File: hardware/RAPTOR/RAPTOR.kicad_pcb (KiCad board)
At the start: 2 copper layers, 101.6 x 53.3 mm, 13 parts, among them P1 Digital, P10 CONN_01X01, P11 CONN_01X01, P12 CONN_01X01, P13 CONN_01X01, P2 Power, P3 Analog, P4 Analog, P5 PWM, P6 PWM, P7 Communication, P8 CONN_01X01, P9 CONN_01X01

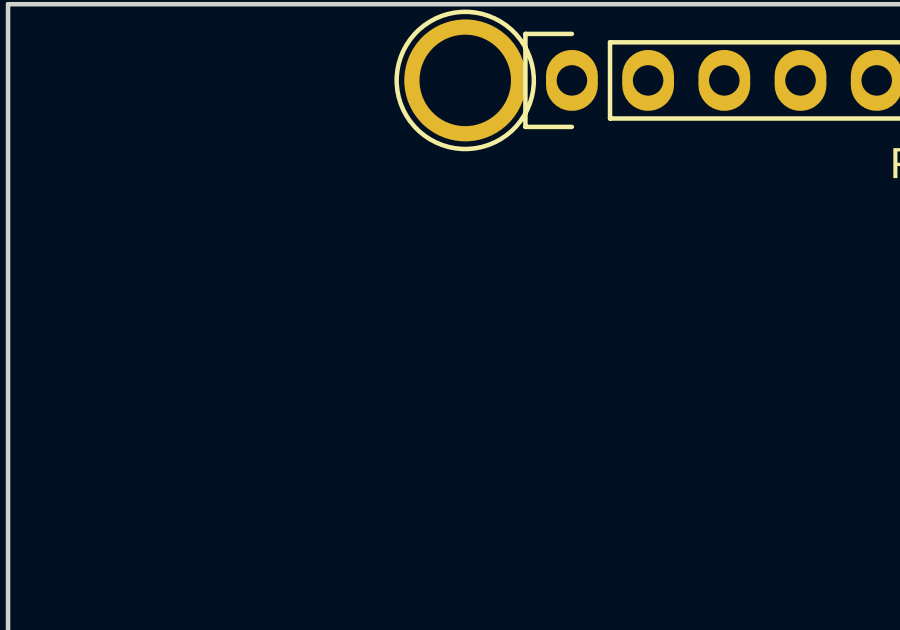
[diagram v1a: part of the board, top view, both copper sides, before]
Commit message: add bmp footprint to pcb
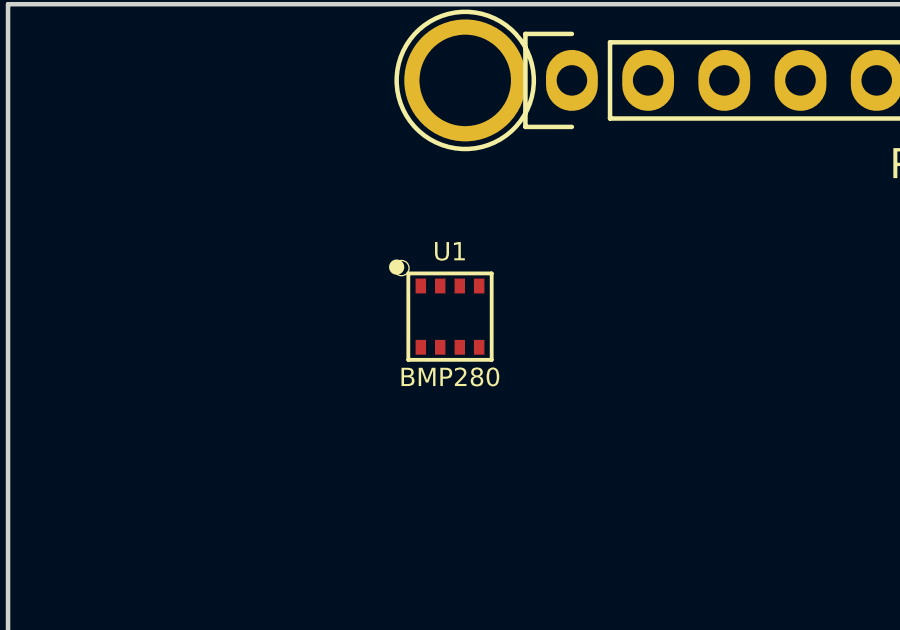
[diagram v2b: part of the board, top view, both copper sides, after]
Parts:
- added U1: BMP280, Silicon-Standard:LGA-8-2.5X2.5, F.Cu at (118.1, 78.7)
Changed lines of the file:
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@@
     (tracks 0)
     (zones 0)
-    (modules 13)
-    (nets 87)
+    (modules 14)
+    (nets 89)
   )
   (page A4)
@@
   (net 85 "/18(Tx1)")
   (net 86 "/19(Rx1)")
+  (net 87 "Net-(U1-Pad2)")
+  (net 88 "Net-(U1-Pad5)")
   (net_class Default "This is the default net class."
     (clearance 0.2)
@@
     (add_net "Net-(P8-Pad1)")
     (add_net "Net-(P9-Pad1)")
+    (add_net "Net-(U1-Pad2)")
+    (add_net "Net-(U1-Pad5)")
   )
   (module Socket_Arduino_Mega:Socket_Strip_Arduino_2x18 locked (layer F.Cu)
@@
       (net 76 "Net-(P13-Pad1)"))
   )
+  (module Silicon-Standard:LGA-8-2.5X2.5 (layer F.Cu)
+    (at 118.11 78.74)
+    (descr "LGA 8-PIN &NDASH;  2.5MM X 2.5MM, 0.65MM PITCH")
+    (tags "LGA 8-PIN &NDASH;  2.5MM X 2.5MM, 0.65MM PITCH")
+    (attr smd)
+    (fp_text reference U1 (at 0 -2.159) (layer F.SilkS)
+      (effects (font (size 0.6096 0.6096) (thickness 0.127)))
+    )
+    (fp_text value BMP280 (at 0 2.032) (layer F.SilkS)
+      (effects (font (size 0.6096 0.6096) (thickness 0.127)))
+    )
+    (fp_circle (center -1.778 -1.651) (end -1.651 -1.651) (layer F.SilkS) (width 0.254))
+    (fp_line (start -1.14808 -0.79756) (end -0.79756 -0.79756) (layer Dwgs.User) (width 0.06604))
+    (fp_line (start -0.79756 -0.79756) (end -0.79756 -1.14808) (layer Dwgs.User) (width 0.06604))
+    (fp_line (start -1.14808 -1.14808) (end -0.79756 -1.14808) (layer Dwgs.User) (width 0.06604))
+    (fp_line (start -1.14808 -0.79756) (end -1.14808 -1.14808) (layer Dwgs.User) (width 0.06604))
+    (fp_line (start -0.49784 -0.79756) (end -0.14986 -0.79756) (layer Dwgs.User) (width 0.06604))
+    (fp_line (start -0.14986 -0.79756) (end -0.14986 -1.14808) (layer Dwgs.User) (width 0.06604))
+    (fp_line (start -0.49784 -1.14808) (end -0.14986 -1.14808) (layer Dwgs.User) (width 0.06604))
+    (fp_line (start -0.49784 -0.79756) (end -0.49784 -1.14808) (layer Dwgs.User) (width 0.06604))
+    (fp_line (start 0.14986 -0.79756) (end 0.49784 -0.79756) (layer Dwgs.User) (width 0.06604))
+    (fp_line (start 0.49784 -0.79756) (end 0.49784 -1.14808) (layer Dwgs.User) (width 0.06604))
+    (fp_line (start 0.14986 -1.14808) (end 0.49784 -1.14808) (layer Dwgs.User) (width 0.06604))
+    (fp_line (start 0.14986 -0.79756) (end 0.14986 -1.14808) (layer Dwgs.User) (width 0.06604))
+    (fp_line (start 0.79756 -0.79756) (end 1.14808 -0.79756) (layer Dwgs.User) (width 0.06604))
+    (fp_line (start 1.14808 -0.79756) (end 1.14808 -1.14808) (layer Dwgs.User) (width 0.06604))
+    (fp_line (start 0.79756 -1.14808) (end 1.14808 -1.14808) (layer Dwgs.User) (width 0.06604))
+    (fp_line (start 0.79756 -0.79756) (end 0.79756 -1.14808) (layer Dwgs.User) (width 0.06604))
+    (fp_line (start -1.14808 1.14808) (end -0.79756 1.14808) (layer Dwgs.User) (width 0.06604))
+    (fp_line (start -0.79756 1.14808) (end -0.79756 0.79756) (layer Dwgs.User) (width 0.06604))
+    (fp_line (start -1.14808 0.79756) (end -0.79756 0.79756) (layer Dwgs.User) (width 0.06604))
+    (fp_line (start -1.14808 1.14808) (end -1.14808 0.79756) (layer Dwgs.User) (width 0.06604))
+    (fp_line (start -0.49784 1.14808) (end -0.14986 1.14808) (layer Dwgs.User) (width 0.06604))
+    (fp_line (start -0.14986 1.14808) (end -0.14986 0.79756) (layer Dwgs.User) (width 0.06604))
+    (fp_line (start -0.49784 0.79756) (end -0.14986 0.79756) (layer Dwgs.User) (width 0.06604))
+    (fp_line (start -0.49784 1.14808) (end -0.49784 0.79756) (layer Dwgs.User) (width 0.06604))
+    (fp_line (start 0.14986 1.14808) (end 0.49784 1.14808) (layer Dwgs.User) (width 0.06604))
+    (fp_line (start 0.49784 1.14808) (end 0.49784 0.79756) (layer Dwgs.User) (width 0.06604))
+    (fp_line (start 0.14986 0.79756) (end 0.49784 0.79756) (layer Dwgs.User) (width 0.06604))
+    (fp_line (start 0.14986 1.14808) (end 0.14986 0.79756) (layer Dwgs.User) (width 0.06604))
+    (fp_line (start 0.79756 1.14808) (end 1.14808 1.14808) (layer Dwgs.User) (width 0.06604))
+    (fp_line (start 1.14808 1.14808) (end 1.14808 0.79756) (layer Dwgs.User) (width 0.06604))
+    (fp_line (start 0.79756 0.79756) (end 1.14808 0.79756) (layer Dwgs.User) (width 0.06604))
+    (fp_line (start 0.79756 1.14808) (end 0.79756 0.79756) (layer Dwgs.User) (width 0.06604))
+    (fp_line (start -1.38938 1.44018) (end -1.38938 -1.44018) (layer F.SilkS) (width 0.127))
+    (fp_line (start -1.38938 -1.44018) (end 1.38938 -1.44018) (layer F.SilkS) (width 0.127))
+    (fp_line (start 1.38938 -1.44018) (end 1.38938 1.44018) (layer F.SilkS) (width 0.127))
+    (fp_line (start 1.38938 1.44018) (end -1.38938 1.44018) (layer F.SilkS) (width 0.127))
+    (fp_line (start 1.24968 1.24968) (end 1.24968 -1.24968) (layer Dwgs.User) (width 0))
+    (fp_line (start 1.24968 -1.24968) (end -1.24968 -1.24968) (layer Dwgs.User) (width 0))
+    (fp_line (start -1.24968 -1.24968) (end -1.24968 1.24968) (layer Dwgs.User) (width 0))
+    (fp_line (start -1.24968 1.24968) (end 1.24968 1.24968) (layer Dwgs.User) (width 0))
+    (fp_circle (center -1.61798 -1.61798) (end -1.61798 -1.87198) (layer F.SilkS) (width 0))
+    (pad 1 smd rect (at -0.97282 -1.02362 90) (size 0.49784 0.34798) (layers F.Cu F.Paste F.Mask)
+      (net 1 GND) (solder_mask_margin 0.1016))
+    (pad 2 smd rect (at -0.32258 -1.02362 90) (size 0.49784 0.34798) (layers F.Cu F.Paste F.Mask)
+      (net 87 "Net-(U1-Pad2)") (solder_mask_margin 0.1016))
+    (pad 3 smd rect (at 0.32258 -1.02362 90) (size 0.49784 0.34798) (layers F.Cu F.Paste F.Mask)
+      (net 69 "/20(SDA)") (solder_mask_margin 0.1016))
+    (pad 4 smd rect (at 0.97282 -1.02362 90) (size 0.49784 0.34798) (layers F.Cu F.Paste F.Mask)
+      (net 70 "/21(SCL)") (solder_mask_margin 0.1016))
+    (pad 5 smd rect (at 0.97282 1.02362 90) (size 0.49784 0.34798) (layers F.Cu F.Paste F.Mask)
+      (net 88 "Net-(U1-Pad5)") (solder_mask_margin 0.1016))
+    (pad 6 smd rect (at 0.32258 1.02362 90) (size 0.49784 0.34798) (layers F.Cu F.Paste F.Mask)
+      (net 34 +5V) (solder_mask_margin 0.1016))
+    (pad 7 smd rect (at -0.32258 1.02362 90) (size 0.49784 0.34798) (layers F.Cu F.Paste F.Mask)
+      (net 1 GND) (solder_mask_margin 0.1016))
+    (pad 8 smd rect (at -0.97282 1.02362 90) (size 0.49784 0.34798) (layers F.Cu F.Paste F.Mask)
+      (net 34 +5V) (solder_mask_margin 0.1016))
+  )
   (gr_text 1 (at 131.318 116.586 90) (layer F.SilkS)

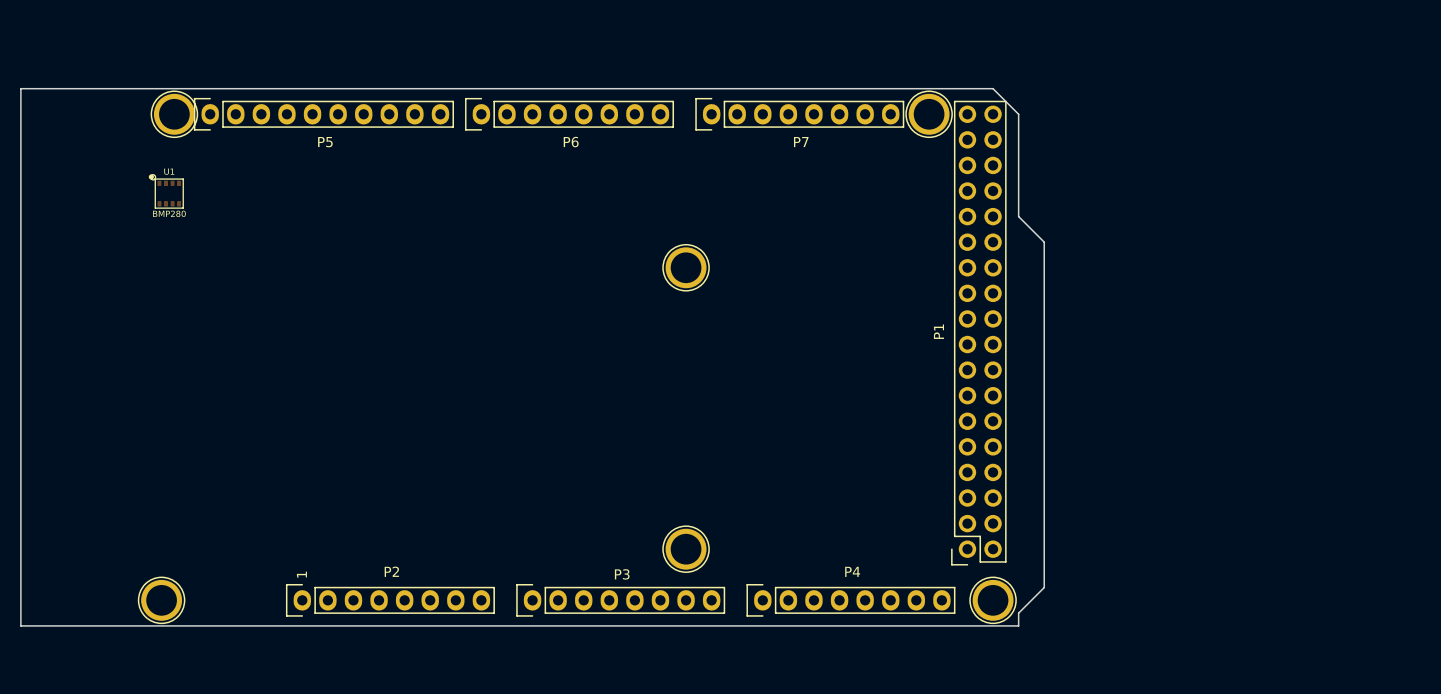
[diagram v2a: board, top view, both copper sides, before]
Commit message: move to uno, re-add bmp
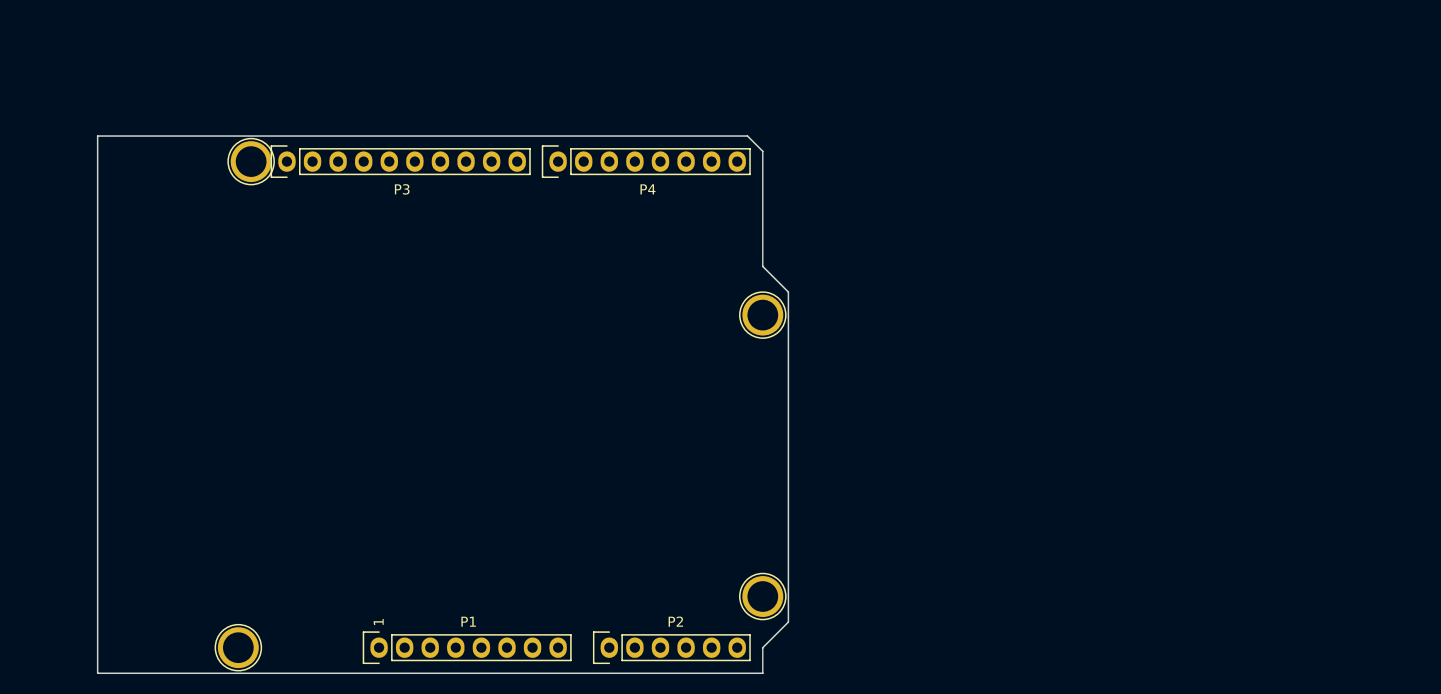
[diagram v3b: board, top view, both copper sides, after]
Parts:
- removed P10, P11, P12, P13, P9: CONN_01X01, Socket_Arduino_Mega:Arduino_1pin
- removed U1: BMP280, Silicon-Standard:LGA-8-2.5X2.5
- P1: value Digital -> Power; footprint Socket_Arduino_Mega:Socket_Strip_Arduino_2x18 -> Socket_Arduino_Uno:Socket_Strip_Arduino_1x08
- P2: value Power -> Analog; footprint Socket_Arduino_Mega:Socket_Strip_Arduino_1x08 -> Socket_Arduino_Uno:Socket_Strip_Arduino_1x06
- P3: value Analog -> Digital; footprint Socket_Arduino_Mega:Socket_Strip_Arduino_1x08 -> Socket_Arduino_Uno:Socket_Strip_Arduino_1x10
- P4: value Analog -> Digital; footprint Socket_Arduino_Mega:Socket_Strip_Arduino_1x08 -> Socket_Arduino_Uno:Socket_Strip_Arduino_1x08
- P5: value PWM -> CONN_01X01; footprint Socket_Arduino_Mega:Socket_Strip_Arduino_1x10 -> Socket_Arduino_Uno:Arduino_1pin
- P6: value PWM -> CONN_01X01; footprint Socket_Arduino_Mega:Socket_Strip_Arduino_1x08 -> Socket_Arduino_Uno:Arduino_1pin
- P7: value Communication -> CONN_01X01; footprint Socket_Arduino_Mega:Socket_Strip_Arduino_1x08 -> Socket_Arduino_Uno:Arduino_1pin
- P8: footprint Socket_Arduino_Mega:Arduino_1pin -> Socket_Arduino_Uno:Arduino_1pin
- moved P8 66.1 mm to (177.0, 90.8)
- moved P1 59.2 mm to (138.9, 123.8), turned to 0 degrees
- moved P6 55.4 mm to (177.0, 118.7)
- moved P5 53.0 mm to (125.0, 123.8)
- moved P3 49.9 mm to (129.8, 75.6)
- moved P4 48.1 mm to (156.7, 75.6)
- moved P7 46.0 mm to (126.2, 75.6)
- moved P2 30.8 mm to (161.8, 123.8)
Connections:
- net /14(Tx3) renamed Net-(P7-Pad1)
- net /7(**) renamed Net-(P6-Pad1)
- net /A11 renamed /4
- net /A13 renamed /2
- net /A14 renamed /1(Tx)
- net /A15 renamed /0(Rx)
- net /A4 renamed /13(SCK)
- net /A5 renamed /12(MISO)
- net /A6 renamed /11(**/MOSI)
- net /A7 renamed /10(**/SS)
- net /A8 renamed /7
- net /SCL renamed Net-(P5-Pad1)
- P1 pad 1: GND -> Net-(P1-Pad1)
- P1 pad 2: GND -> /IOREF
- P1 pad 3: /52(SCK) -> /Reset
- P1 pad 4: /53(SS) -> +3V3
- P1 pad 5: /50(MISO) -> +5V
- P1 pad 6: /51(MOSI) -> GND
- P1 pad 7: /48 -> GND
- P1 pad 8: /49 -> /Vin
- P2 pad 1: Net-(P2-Pad1) -> /A0
- P2 pad 2: /IOREF -> /A1
- P2 pad 3: /Reset -> /A2
- P2 pad 4: +3V3 -> /A3
- P2 pad 5: +5V -> /A4(SDA)
- P2 pad 6: GND -> /A5(SCL)
- P3 pad 1: /A0 -> /A5(SCL)
- P3 pad 2: /A1 -> /A4(SDA)
- P3 pad 3: /A2 -> /AREF
- P3 pad 4: /A3 -> GND
- P4 pad 2: /A9 -> /6(**)
- P4 pad 3: /A10 -> /5(**)
- P4 pad 5: /A12 -> /3(**)
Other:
- board size 101.6 x 53.3 mm -> 68.6 x 53.3 mm

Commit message: Added all the footprints and associated them with the symbols in the schematics
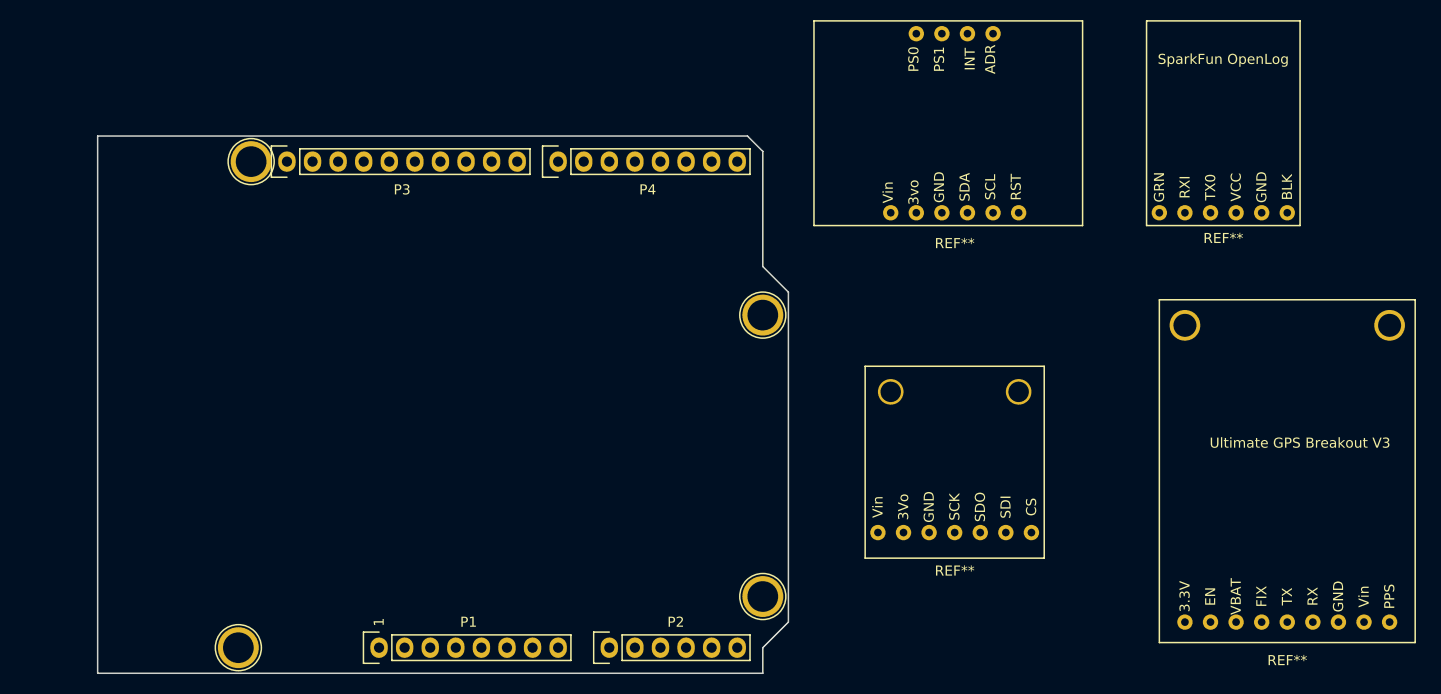
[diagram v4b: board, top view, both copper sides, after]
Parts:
- added REF**: BNO055, RAPTOR_footprints:BNO055, F.Cu at (196.1, 80.6)
- added REF**: OpenLog, RAPTOR_footprints:OpenLog, F.Cu at (221.5, 80.6)
- added REF**: BMP280, RAPTOR_footprints:BMP280, F.Cu at (196.1, 112.4)
- added REF**: Adafruit GPS, RAPTOR_footprints:AdafruitGPS, F.Cu at (229.1, 121.3)
